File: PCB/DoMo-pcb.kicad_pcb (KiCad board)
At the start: 2 copper layers, 32 parts, among them SW0 SW_Push, SW1 Rotary_Encoder_Switch, SW10 SW_Push, SW2 SW_Push, SW3 SW_Push, SW4 SW_Push, SW5 SW_Push, SW6 SW_Push, SW7 SW_Push, SW8 SW_Push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

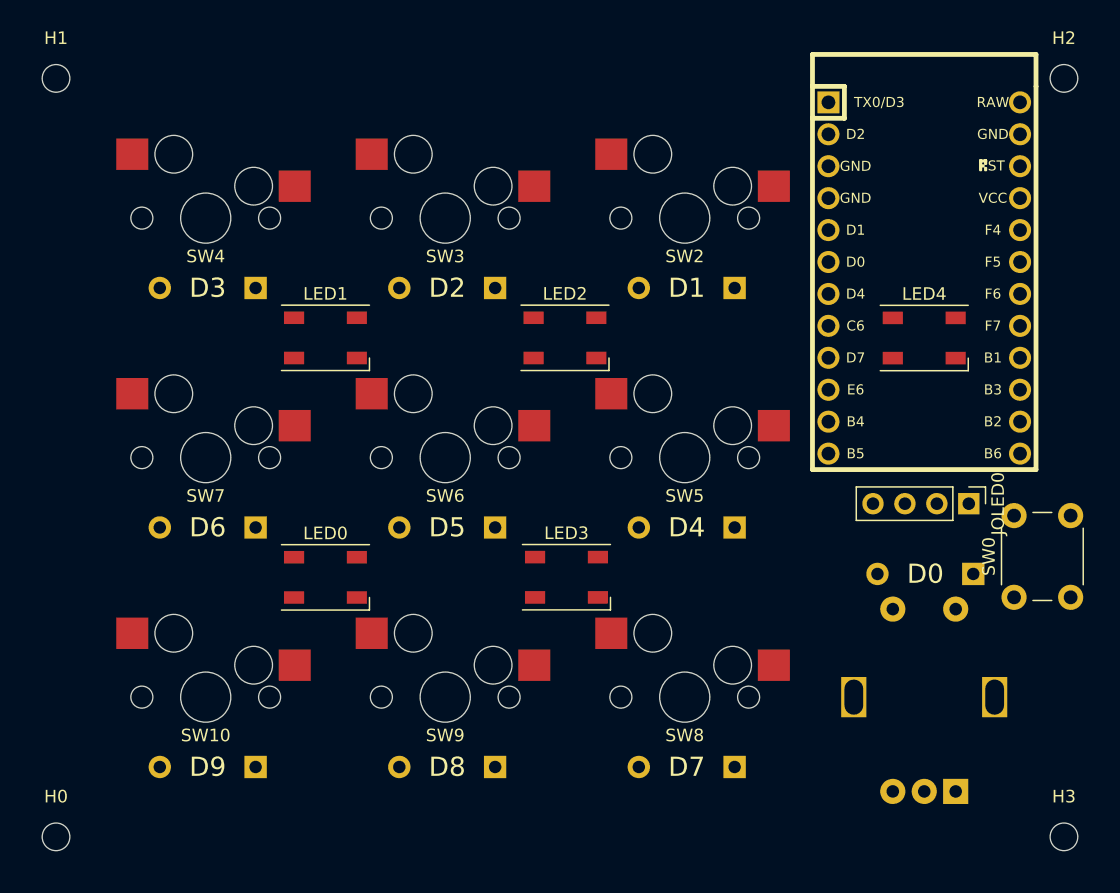
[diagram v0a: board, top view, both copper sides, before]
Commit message: remove 1 led and wire up oled/rotary
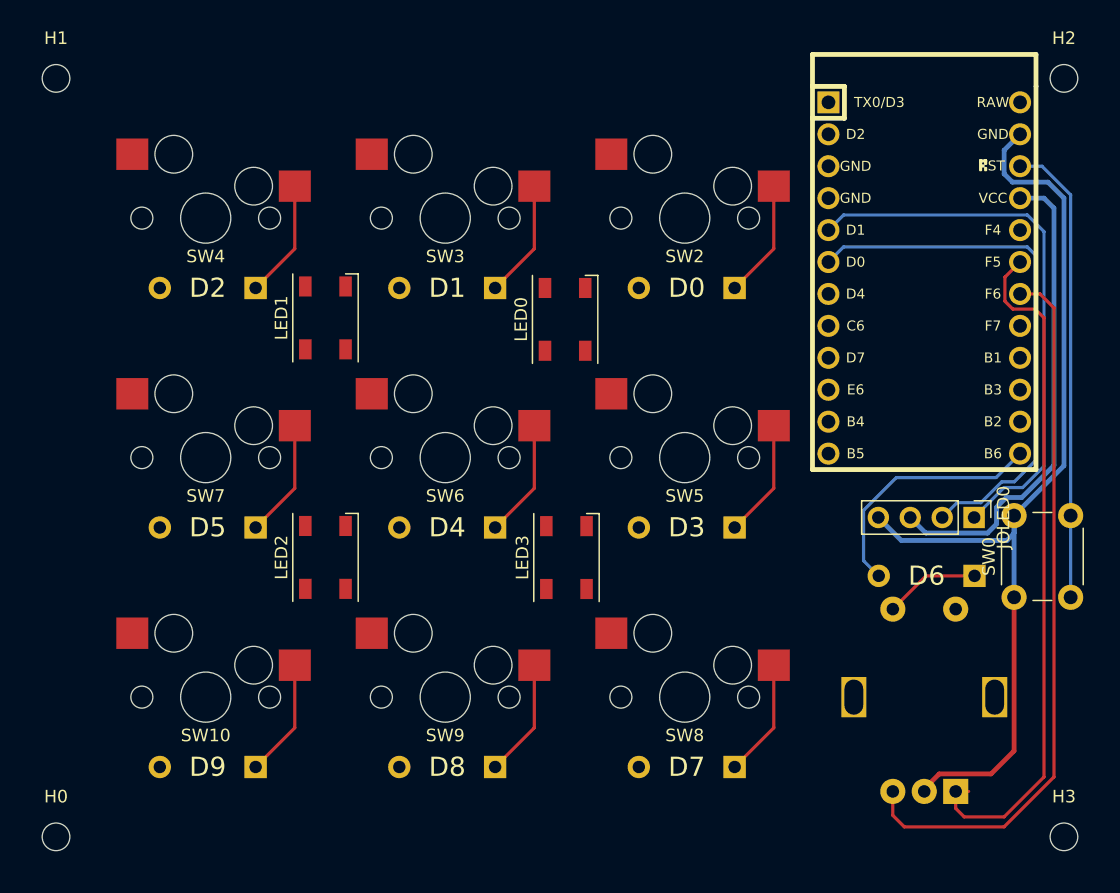
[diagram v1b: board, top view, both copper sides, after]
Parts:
- removed LED4: WS2812B, LEDs:LED_WS2812B-PLCC4
- moved D6 57.3 mm to (243.1, 92.4)
- moved D3 42.6 mm to (224.0, 88.6)
- moved D0 29.6 mm to (224.0, 69.5)
- moved LED0 28.0 mm to (214.3, 77.1), turned to 90 degrees
- moved LED2 25.8 mm to (195.3, 96.0), turned to 90 degrees
- moved D1 19.1 mm to (204.9, 69.5)
- moved D4 19.1 mm to (204.9, 88.6)
- moved D2 19.0 mm to (185.9, 69.5)
- moved D5 19.0 mm to (185.9, 88.6)
- moved LED1 1.59 mm to (195.3, 77.0), turned to 90 degrees
- moved LED3 1.56 mm to (214.4, 96.1), turned to 90 degrees
- moved JOLED0 1.18 mm to (246.9, 92.9)
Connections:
- U0 pad 10: R0 -> C1
- U0 pad 11: R1 -> C2
- U0 pad 12: R2 -> C3
- U0 pad 13: C3 -> R2
- U0 pad 14: C2 -> R1
- U0 pad 15: C1 -> R0
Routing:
- net GND: track 0.00 -> 76.6 mm
- net EN1: track 0.00 -> 57.2 mm
- net EN0: track 0.00 -> 54.8 mm
- net SDA: track 0.00 -> 44.1 mm
- net SCL: track 0.00 -> 42.9 mm
- net VCC: track 0.00 -> 38.4 mm
- net RST: track 0.00 -> 37.0 mm
- net R2: track 0.00 -> 20.0 mm
- net Net-(D8-Pad2): track 0.00 -> 9.39 mm
- net Net-(D7-Pad2): track 0.00 -> 9.39 mm
- net Net-(D4-Pad2): track 0.00 -> 9.39 mm
- net Net-(D3-Pad2): track 0.00 -> 9.39 mm
- net Net-(D1-Pad2): track 0.00 -> 9.39 mm
- net Net-(D0-Pad2): track 0.00 -> 9.39 mm
- net Net-(D9-Pad2): track 0.00 -> 9.39 mm
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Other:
- net class Default: trace_width 0.25 -> 0.254
- net class Power added: clearance 0.2, trace_width 0.381, via_dia 0.8, via_drill 0.4

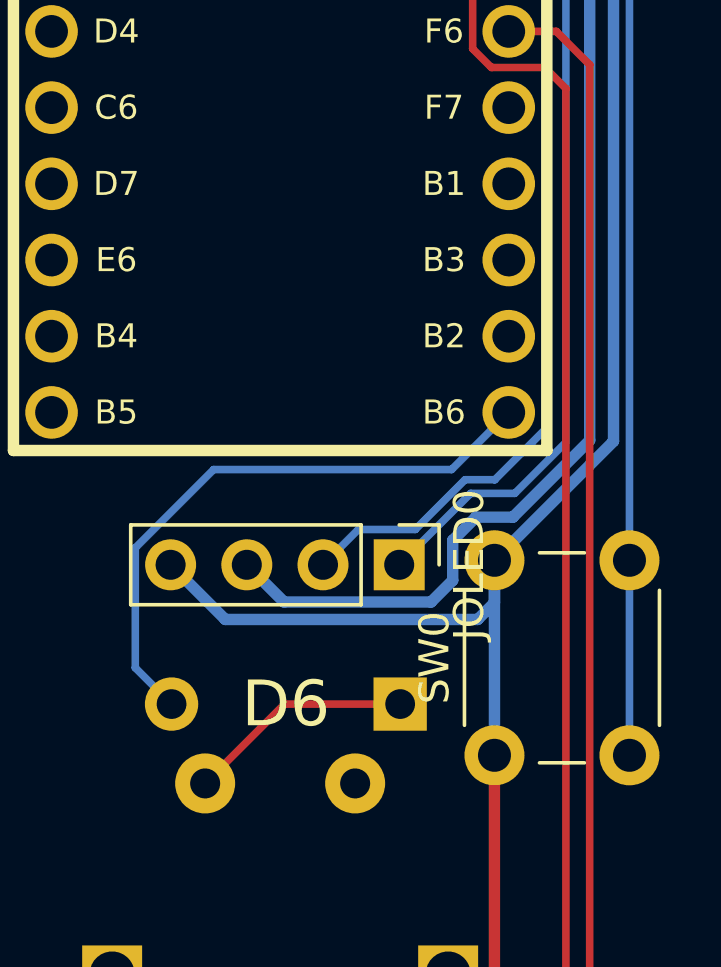
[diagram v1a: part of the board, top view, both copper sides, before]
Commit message: rotary and oled wired up
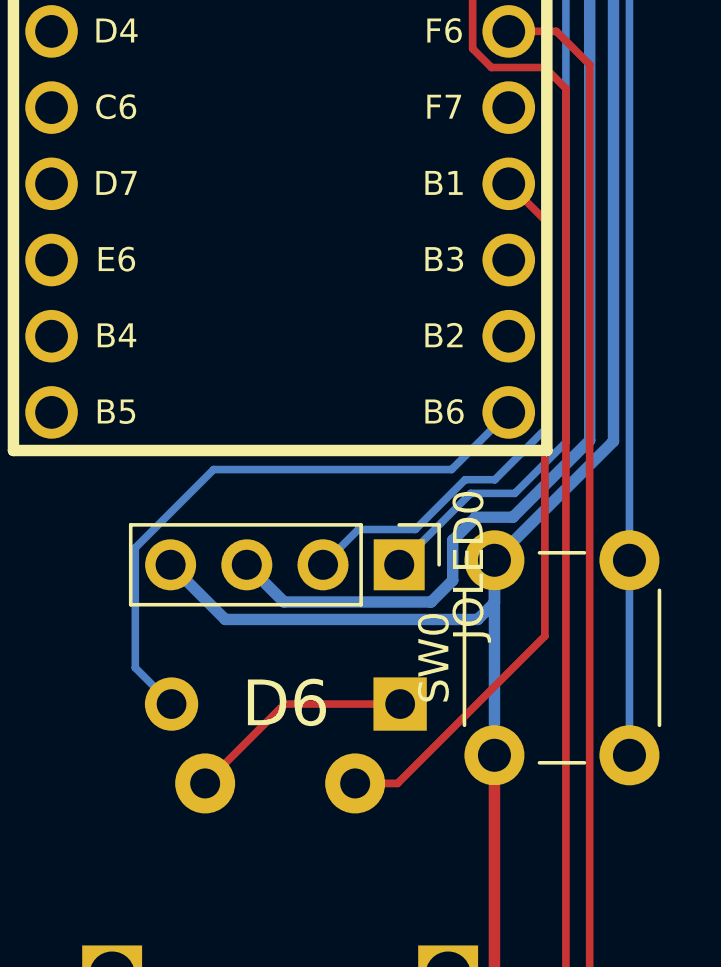
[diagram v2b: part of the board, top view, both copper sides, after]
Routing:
- net C0: track 0.00 -> 23.9 mm
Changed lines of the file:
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@@
     (thickness 1.6)
     (drawings 9)
-    (tracks 91)
+    (tracks 95)
     (zones 0)
     (modules 31)
@@
   (segment (start 254.53125 67.20625) (end 254.53125 92.71875) (width 0.254) (layer B.Cu) (net 23))
   (segment (start 252.25375 64.92875) (end 254.53125 67.20625) (width 0.254) (layer B.Cu) (net 23))
+  (segment (start 251.710801 81.372051) (end 250.5075 80.16875) (width 0.254) (layer F.Cu) (net 24))
+  (segment (start 246.801713 100.15625) (end 251.710801 95.247162) (width 0.254) (layer F.Cu) (net 24))
+  (segment (start 251.710801 95.247162) (end 251.710801 81.372051) (width 0.254) (layer F.Cu) (net 24))
+  (segment (start 245.3875 100.15625) (end 246.801713 100.15625) (width 0.254) (layer F.Cu) (net 24))
   (segment (start 240.3875 116.5625) (end 240.3875 114.65625) (width 0.254) (layer F.Cu) (net 25))
   (segment (start 249.2375 117.475) (end 241.3 117.475) (width 0.254) (layer F.Cu) (net 25))

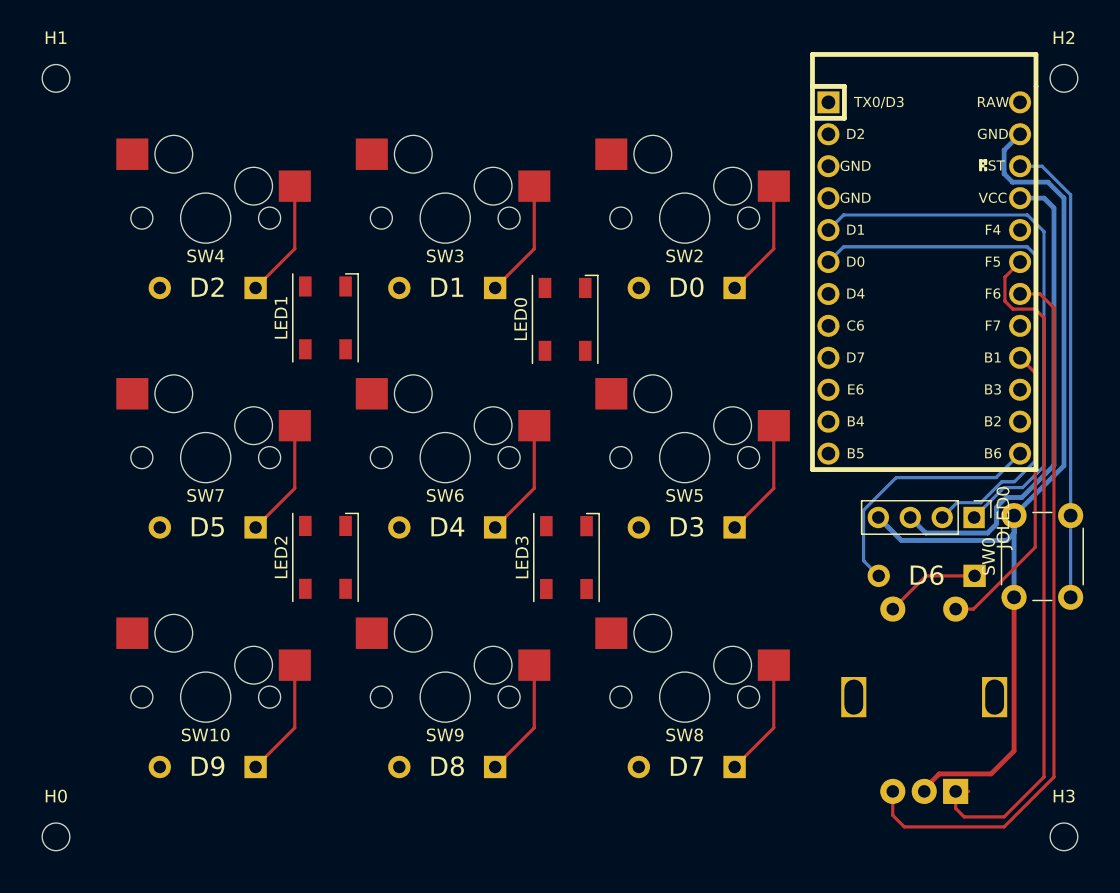
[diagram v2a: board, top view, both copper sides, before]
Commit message: wire up col and row
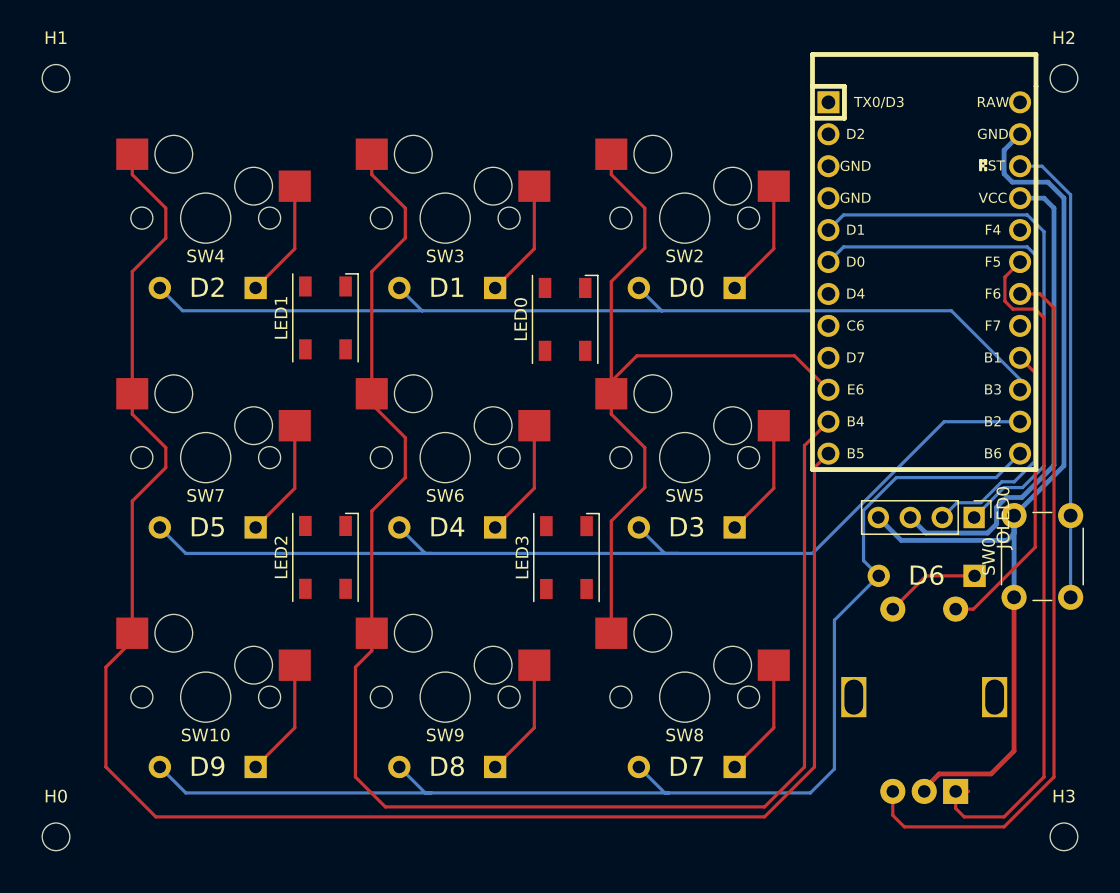
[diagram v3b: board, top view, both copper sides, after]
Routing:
- net C3: track 0.00 -> 139.1 mm
- net C2: track 0.00 -> 120.8 mm
- net R1: track 0.00 -> 81.0 mm
- net R2: track 20.0 -> 98.8 mm
- net R0: track 0.00 -> 77.4 mm
- net C1: track 0.00 -> 62.7 mm

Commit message: wire up leds
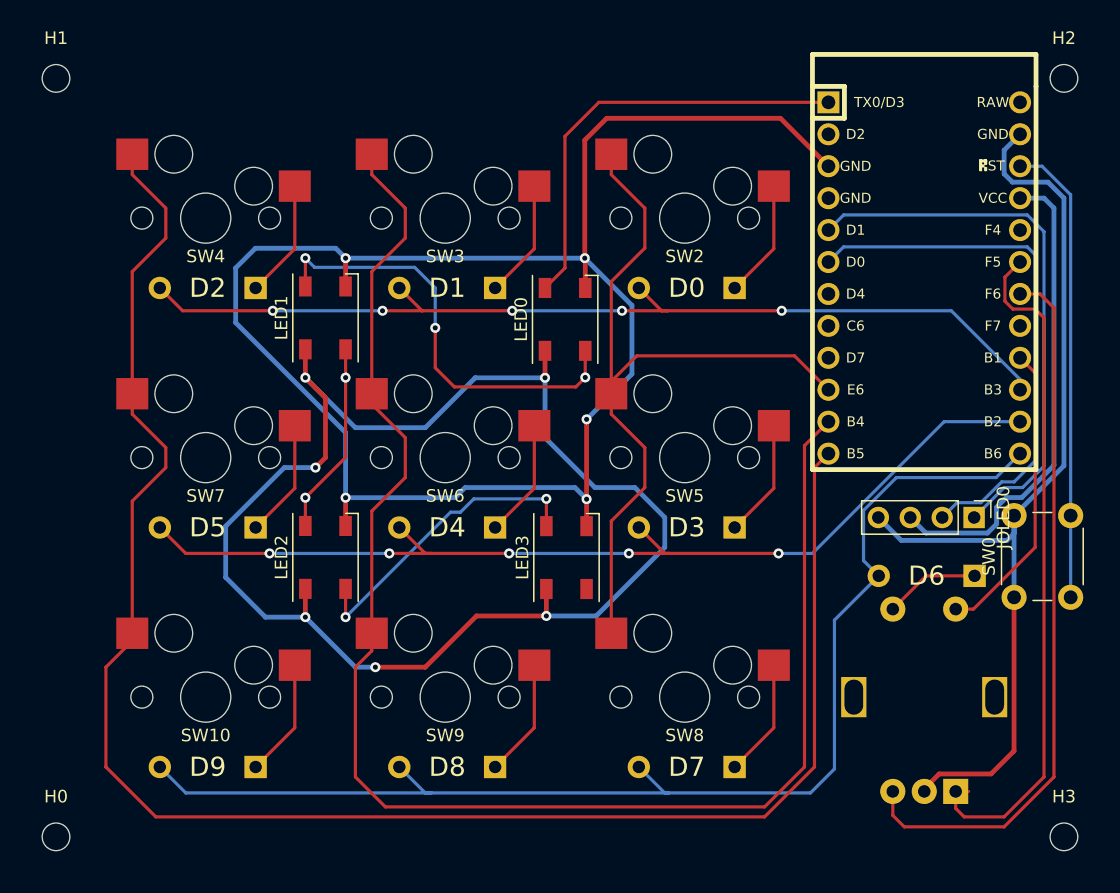
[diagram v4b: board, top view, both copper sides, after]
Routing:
- net GND: track 76.6 -> 209.4 mm, vias 0 -> 5
- net VCC: track 38.4 -> 152.0 mm, vias 0 -> 6
- net Net-(LED0-Pad2): track 0.00 -> 34.9 mm, vias 0 -> 3
- net LEDS: track 0.00 -> 34.8 mm
- net Net-(LED2-Pad2): track 0.00 -> 24.3 mm, vias 0 -> 2
- net Net-(LED1-Pad2): track 0.00 -> 15.4 mm, vias 0 -> 2
- net R1: track 81.0 -> 80.3 mm, vias 0 -> 5
- net R0: track 77.4 -> 77.9 mm, vias 0 -> 5

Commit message: remove unconnected routes
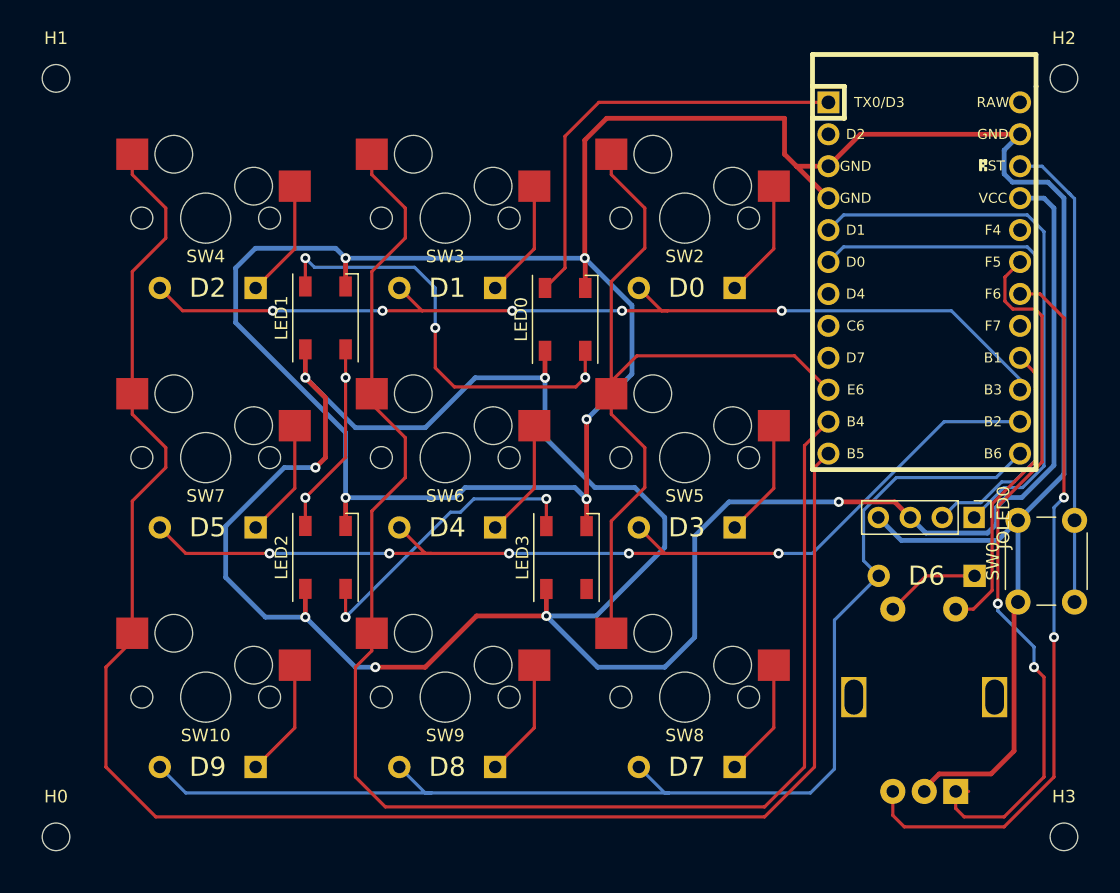
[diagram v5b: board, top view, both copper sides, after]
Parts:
- moved SW0 0.49 mm to (250.3, 99.6)
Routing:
- net VCC: track 152.0 -> 193.3 mm, vias 6 -> 7
- net GND: track 209.4 -> 230.3 mm
- net EN0: track 54.8 -> 57.7 mm, vias 0 -> 2
- net RST: track 37.0 -> 37.7 mm
- net EN1: track 57.2 -> 57.9 mm, vias 0 -> 2

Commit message: ground fill
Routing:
- added copper zone on B.Cu, net GND
- added copper zone on F.Cu, net GND
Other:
- board text added: "DoMo v1.0"
- board text added: "May Do"

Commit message: fix edges
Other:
- board outline added: 84.9 x 65.1 mm
